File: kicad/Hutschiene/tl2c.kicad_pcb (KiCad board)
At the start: 4 copper layers, 175.9 x 86.5 mm, 86 parts, among them IC101 ATTINY20-X, P101 12VDC, P102 RJ45, P103 CTL CONN, P104 TPI Header, P105 DRV CONN, P106 240VAC, P108 UG, P109 5VDC, P110 EG, P111 OG, P201 Mode_Bridge, P501 CONN_PIR_OG, P502 CONN_PIR_EG, P503 CONN_PIR_UG, Q301 IRLML2502, Q302 IRLML2502, Q303 IRLML2502, Q401 IRLML2502, Q402 IRLML2502, Q403 IRLML2502, SW101 TL3315NF160Q, U201 LF120ABDT-TR, U202 TPS70933

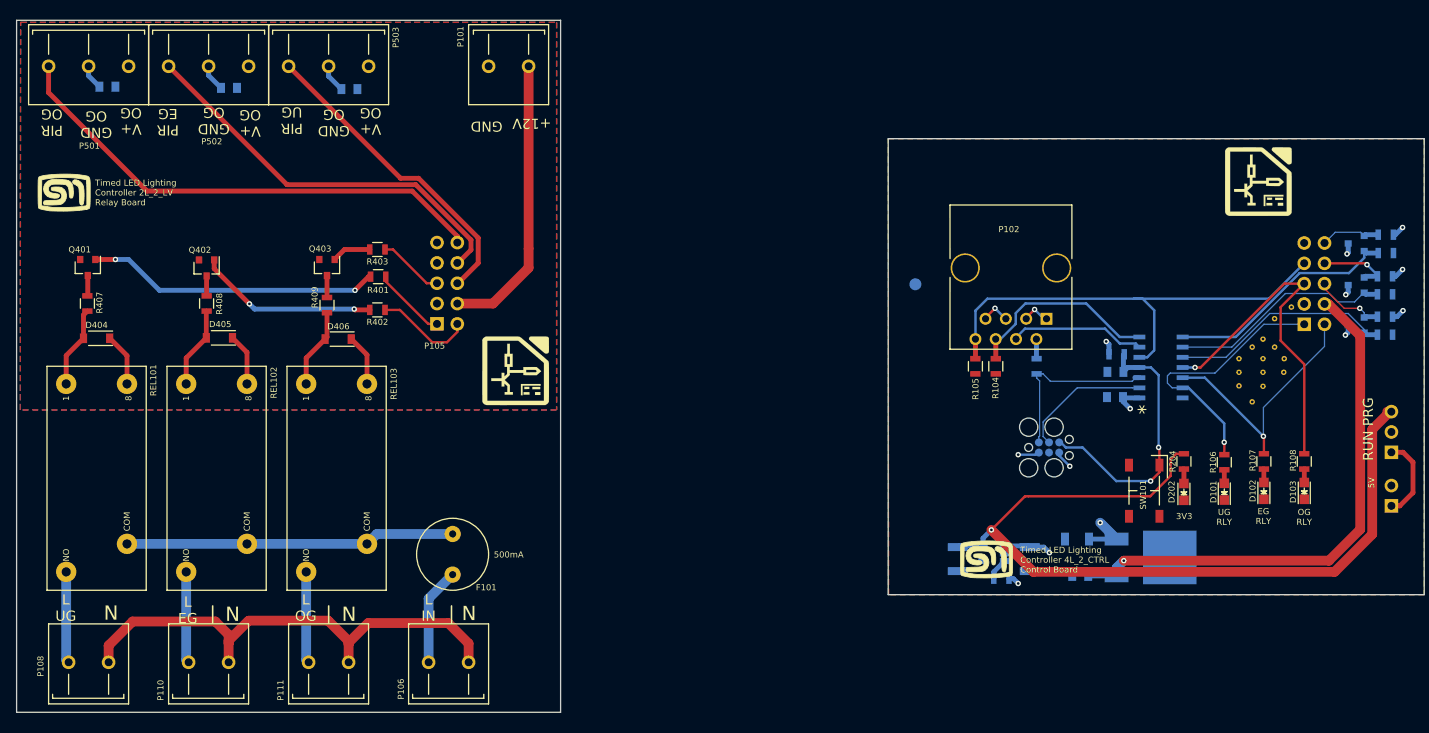
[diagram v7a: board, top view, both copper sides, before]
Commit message: Adjusted the size and location of the terminal blocks
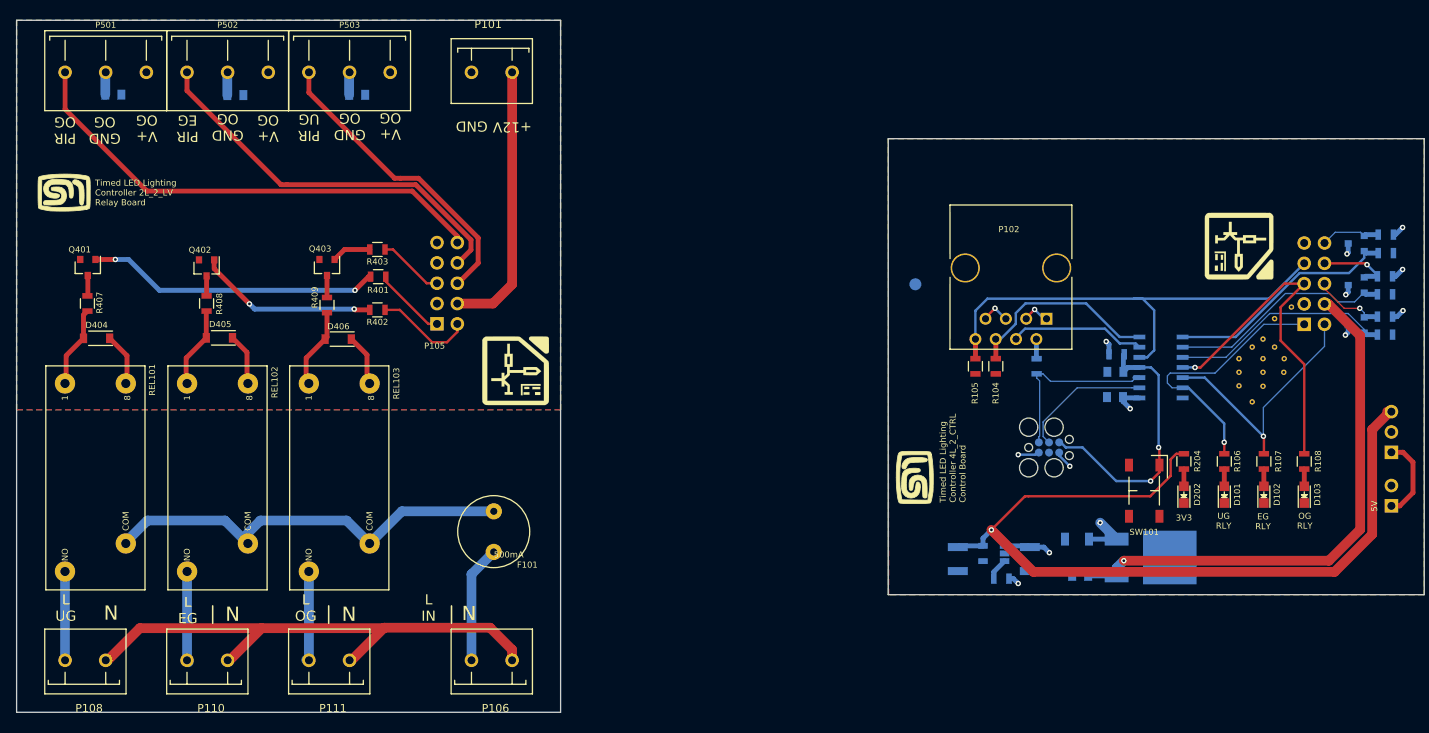
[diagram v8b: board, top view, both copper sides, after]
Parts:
- P101, P106, P108, P110, P111: footprint tl2c-footprint:PCB_Screw_Terminal_Block_5mm_x_2 -> tl2c-footprint:PCB_Screw_Terminal_Block_5.08mm_x_2
- P501, P502, P503: footprint tl2c-footprint:PCB_Screw_Terminal_Block_5mm_x_3 -> tl2c-footprint:PCB_Screw_Terminal_Block_5.8mm_x_3
- moved G*** 59.1 mm to (208.0, 122.4)
- moved G*** 51.0 mm to (160.0, 77.8), turned to 0 degrees
- moved G*** 13.6 mm to (158.0, 117.0), turned to 90 degrees
- moved G*** 8.47 mm to (198.7, 88.0), turned to 270 degrees
- moved F101 5.87 mm to (105.4, 123.7)
- moved P106 5.37 mm to (102.6, 139.8)
- moved P503 2.73 mm to (87.4, 66.3)
- moved P502 2.50 mm to (72.1, 66.3)
- moved P501 2.27 mm to (56.9, 66.3)
- moved P101 2.19 mm to (107.7, 66.3)
- moved C501 1.24 mm to (57.8, 69.1)
- moved C502 1.21 mm to (88.3, 69.1)
- moved C503 1.20 mm to (73.1, 69.2)
- moved P108 0.51 mm to (51.8, 139.8)
- moved D102 0.47 mm to (201.7, 119.1)
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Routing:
- net Net-(F101-Pad2): track 41.2 -> 53.3 mm
- net /Neutral: track 62.2 -> 67.4 mm
- net /Lin: track 12.2 -> 14.7 mm
- net /PIR_Connector/PIR_OG: track 62.6 -> 61.0 mm
- net /DRV_PWR_IN: track 36.0 -> 34.4 mm
- net GNDA: track 9.96 -> 8.53 mm
- net /PIR_Connector/PIR_UG: track 39.9 -> 38.5 mm
- net /PIR_Connector/PIR_EG: track 51.0 -> 49.7 mm
